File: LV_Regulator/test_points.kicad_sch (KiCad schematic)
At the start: 51 parts

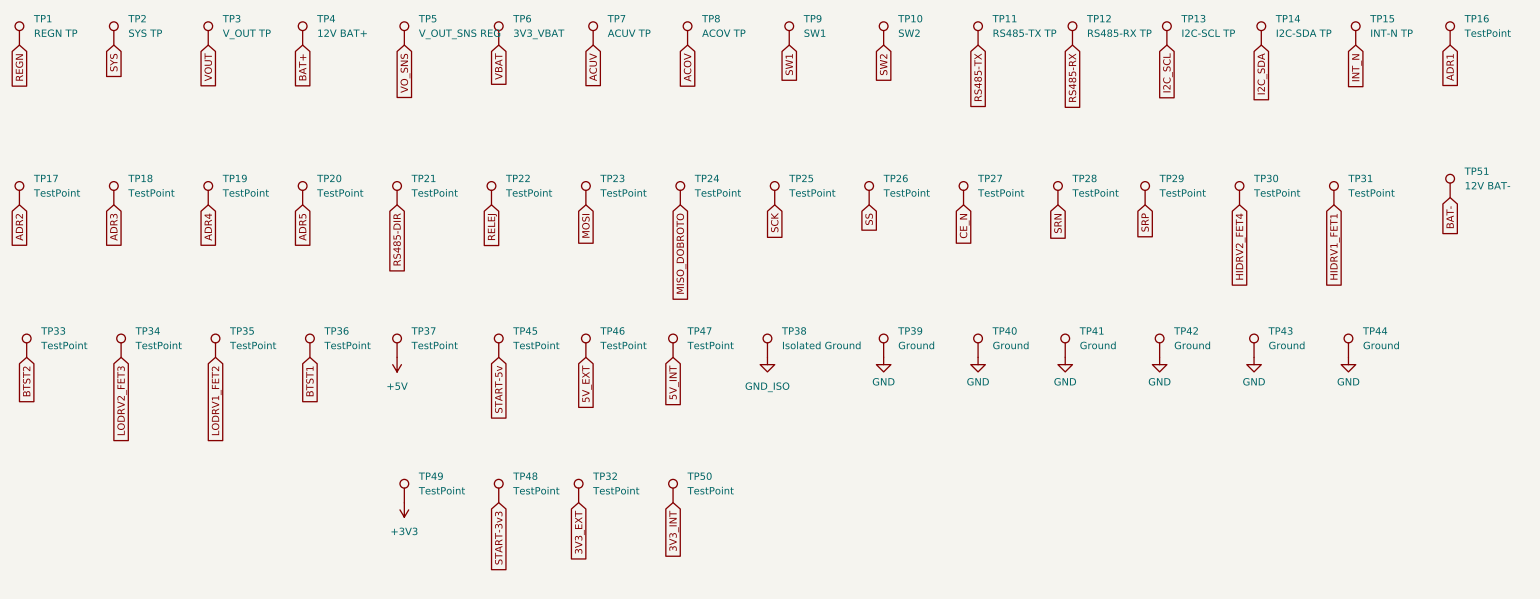
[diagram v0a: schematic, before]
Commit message: Redesigned the control section of the LV_Regulator
The routing of the control section was redone completely, LED's were labeled with their function, some signals were renamed for consistency, removed redundant testpoints, removed names of testpoints, changed configuration jumpers to have human reada
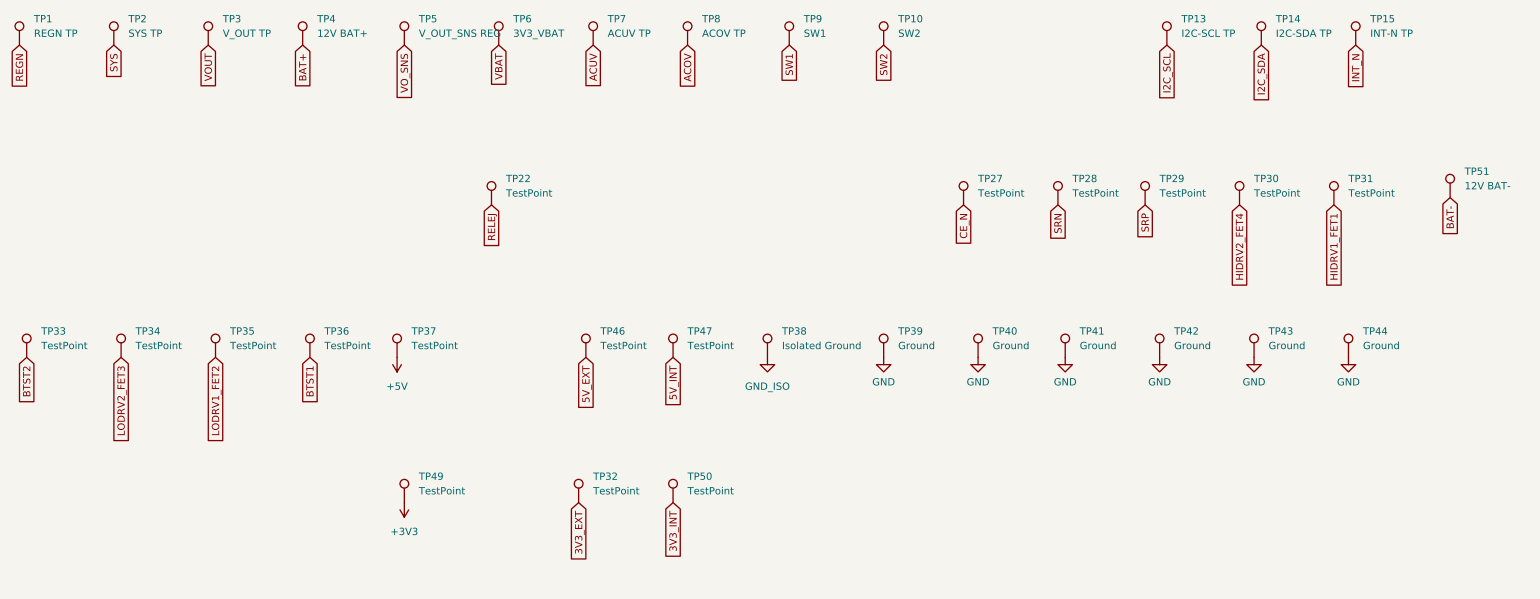
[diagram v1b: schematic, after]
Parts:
- removed TP11: RS485-TX TP, TestPoint:TestPoint_Pad_1.0x1.0mm, symbol Connector:TestPoint
- removed TP12: RS485-RX TP, TestPoint:TestPoint_Pad_1.0x1.0mm, symbol Connector:TestPoint
- removed TP16, TP17, TP18, TP19, TP20, TP21, TP23, TP24, TP25, TP26, TP45, TP48: TestPoint, TestPoint:TestPoint_Pad_1.0x1.0mm, symbol Connector:TestPoint
